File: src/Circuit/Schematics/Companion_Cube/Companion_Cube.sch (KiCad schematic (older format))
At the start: 15 parts

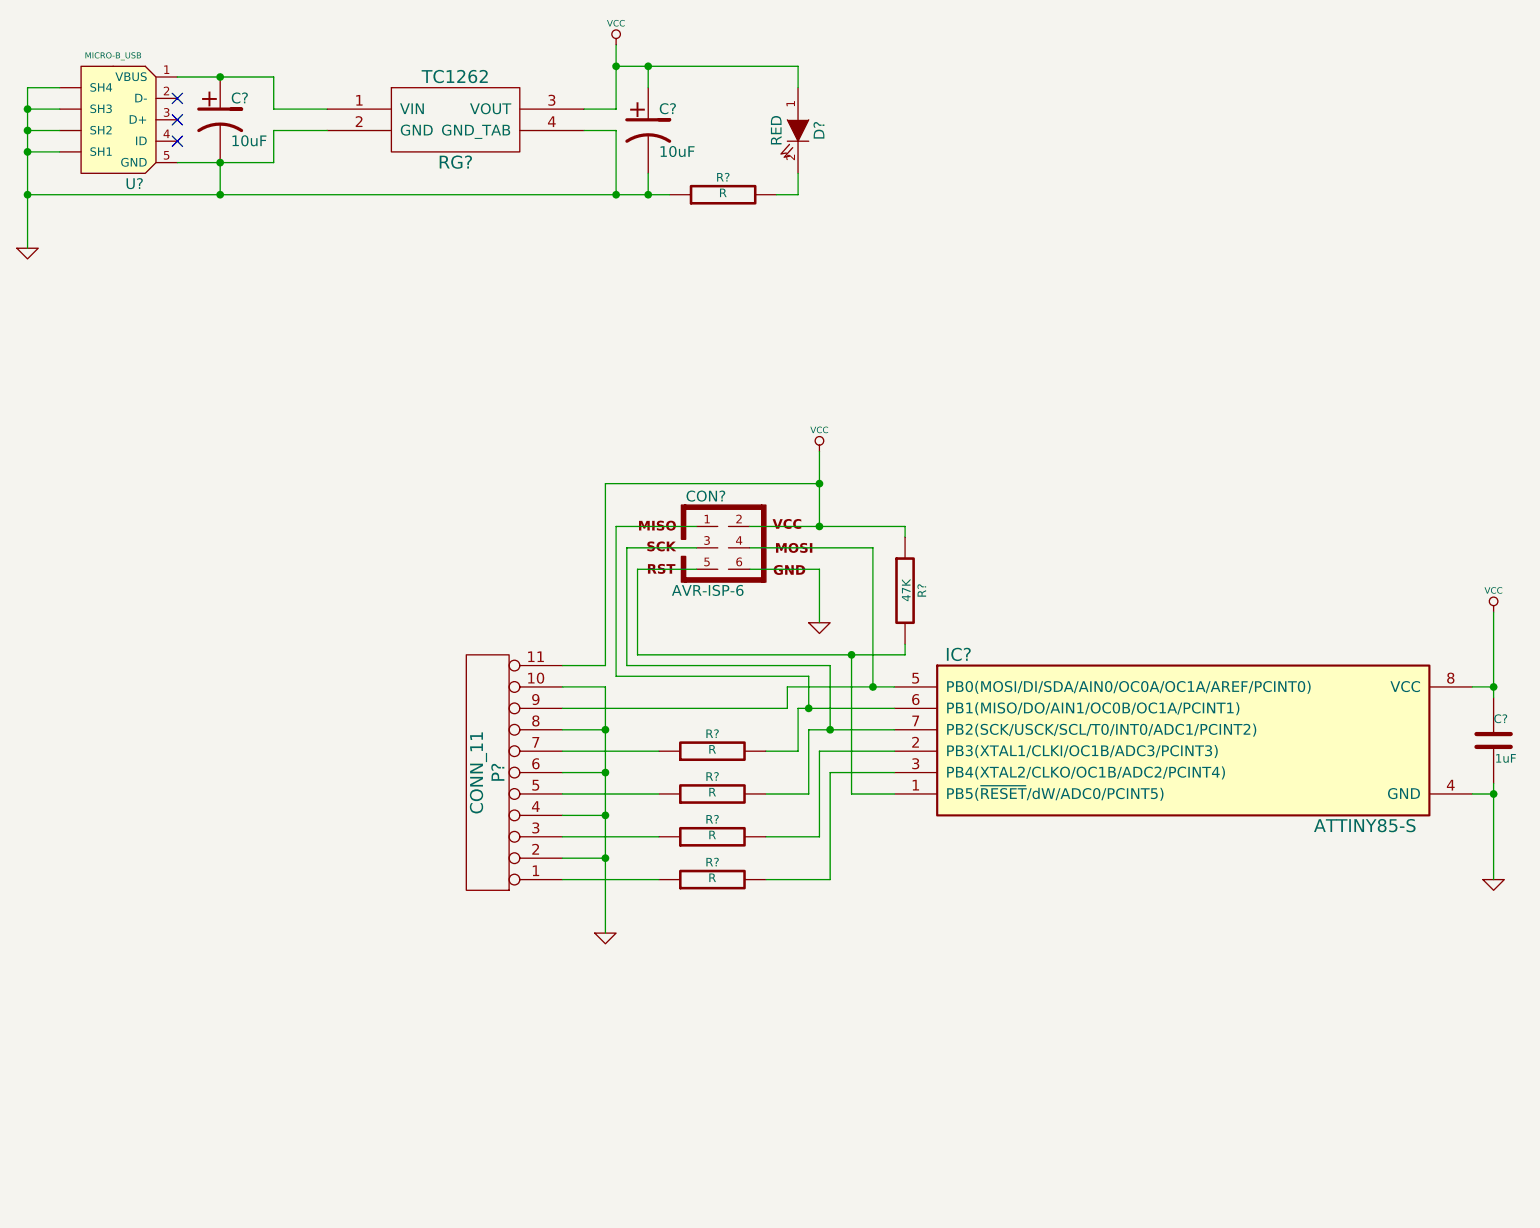
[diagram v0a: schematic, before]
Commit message: Initial LED driver circuit
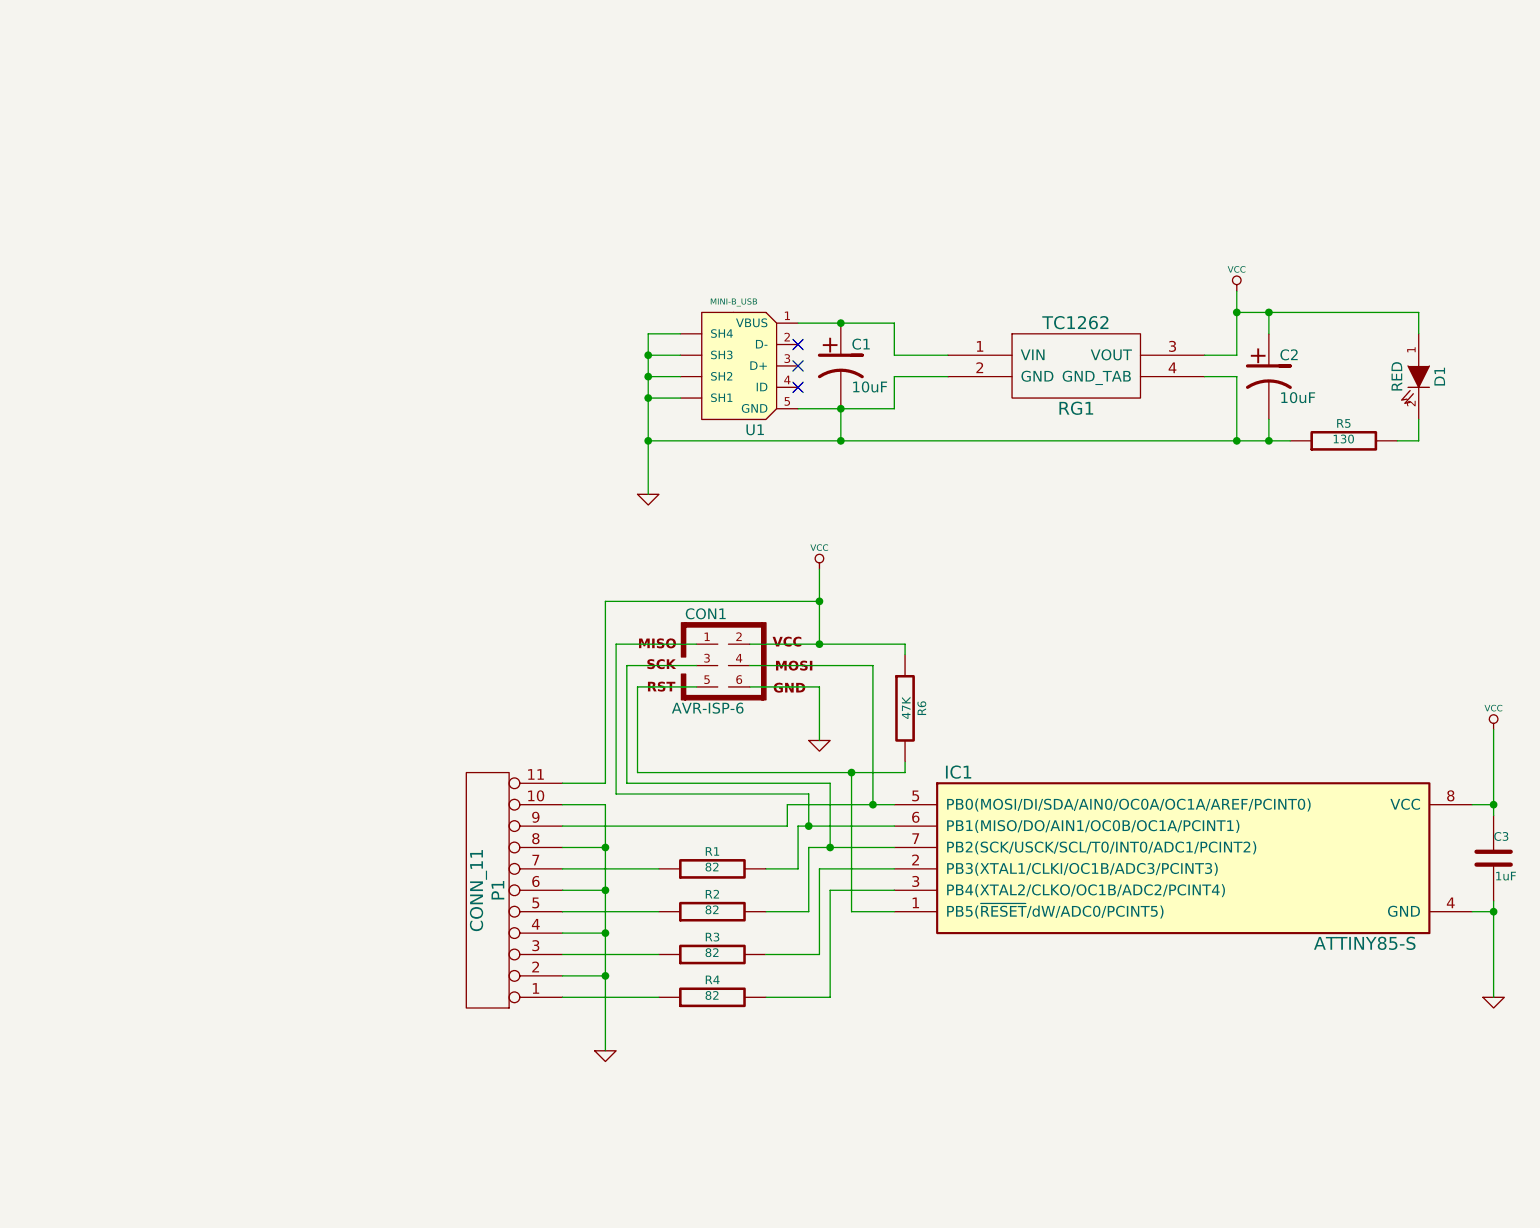
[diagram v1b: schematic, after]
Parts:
- R1, R2, R3, R4: renamed from R?; value R -> 82
- R5: renamed from R?; value R -> 130
- U1: renamed from U?; value MICRO-B_USB -> MINI-B_USB
- gave numbers to parts that had none: 9
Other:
- moved on the sheet: C1, C2, C3, CON1, D1, IC1, P1, R1, R2, R3, R4, R5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

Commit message: Redesigning circuit board for new model
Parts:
- removed P1: CONN_11, ~, symbol CONN_11
- added P1: LED_4, ~, symbol CONN_2
- added P2: LED_3, ~, symbol CONN_2
- added P3: LED_2, ~, symbol CONN_2
- added P4: LED_1, ~, symbol CONN_2
- added P5, P6, P7: CONN_1, ~, symbol CONN_1
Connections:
- net GND: now also P1.1 (P1), P2.1 (P1), P3.1 (P1), P4.1 (P1), P6.1
- net VCC: now also P5.1
- net at CON1.4, IC1.5 (PB0(MOSI/DI/SDA/AIN0/OC0A/OC1A/AREF/PCINT0)): now also P7.1
- net at R4.1: now also P4.2 (PM)
- net at R3.1: now also P3.2 (PM)
- net at R2.1: now also P2.2 (PM)
- net at R1.1: now also P1.2 (PM)
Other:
- moved on the sheet: R2, R3, R4
